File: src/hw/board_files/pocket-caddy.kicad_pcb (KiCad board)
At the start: 4 copper layers, 89 parts, among them J1 Conn_01x03_Pin, J2 Conn_01x03_Pin, J3 MSD-1-A, J4 Test_Points, P1 USB_C_Plug_USB2.0, Q1 PMOS, SW1 SW_PWR, SW2 RESET, SW3 BTN_2, SW4 BTN_1_BOOT, SW5 BTN_3, U1 FT234XD-R, U2 MCP73871, U3 TPS63031DSKR, U4 ESP32-C3-WROOM-02, U5 NEO-M9N, U6 BQ27427, U7 SHT30-DIS, Y1 32.768kHz

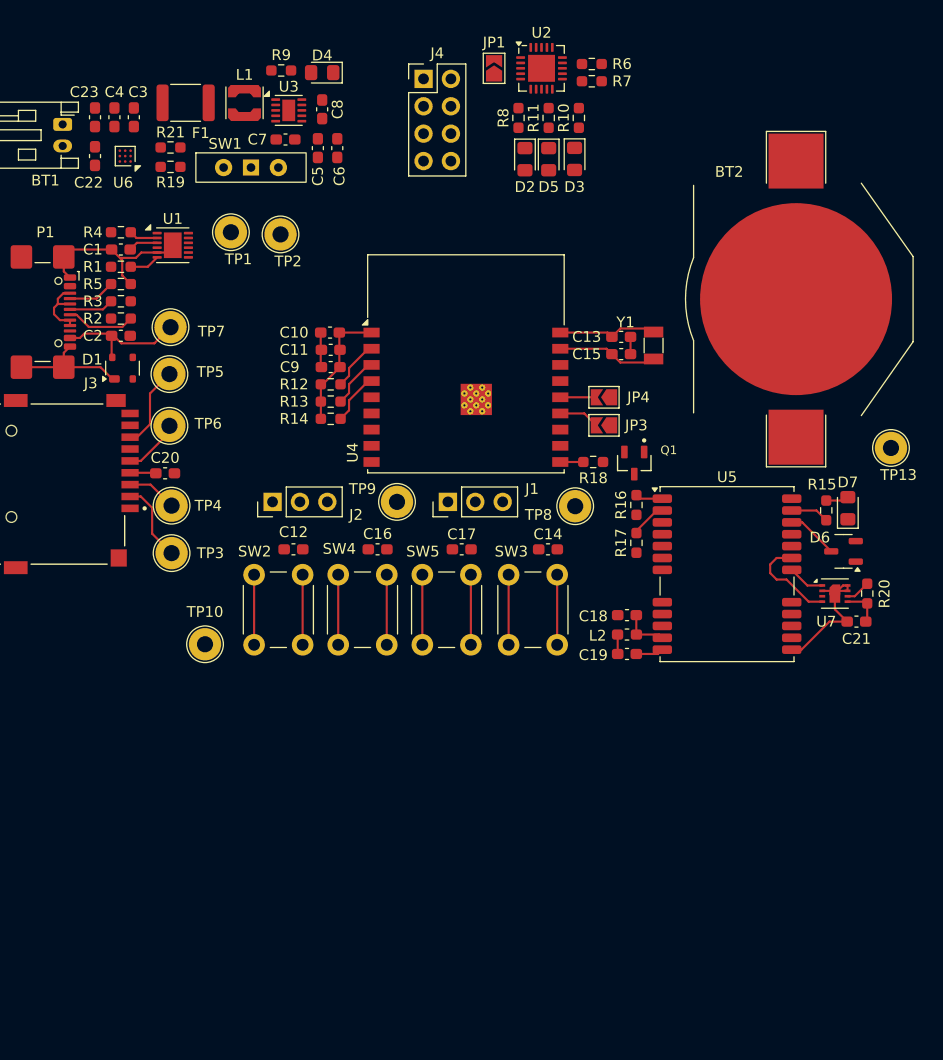
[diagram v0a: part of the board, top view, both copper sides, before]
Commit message: Added LCD to Schematic
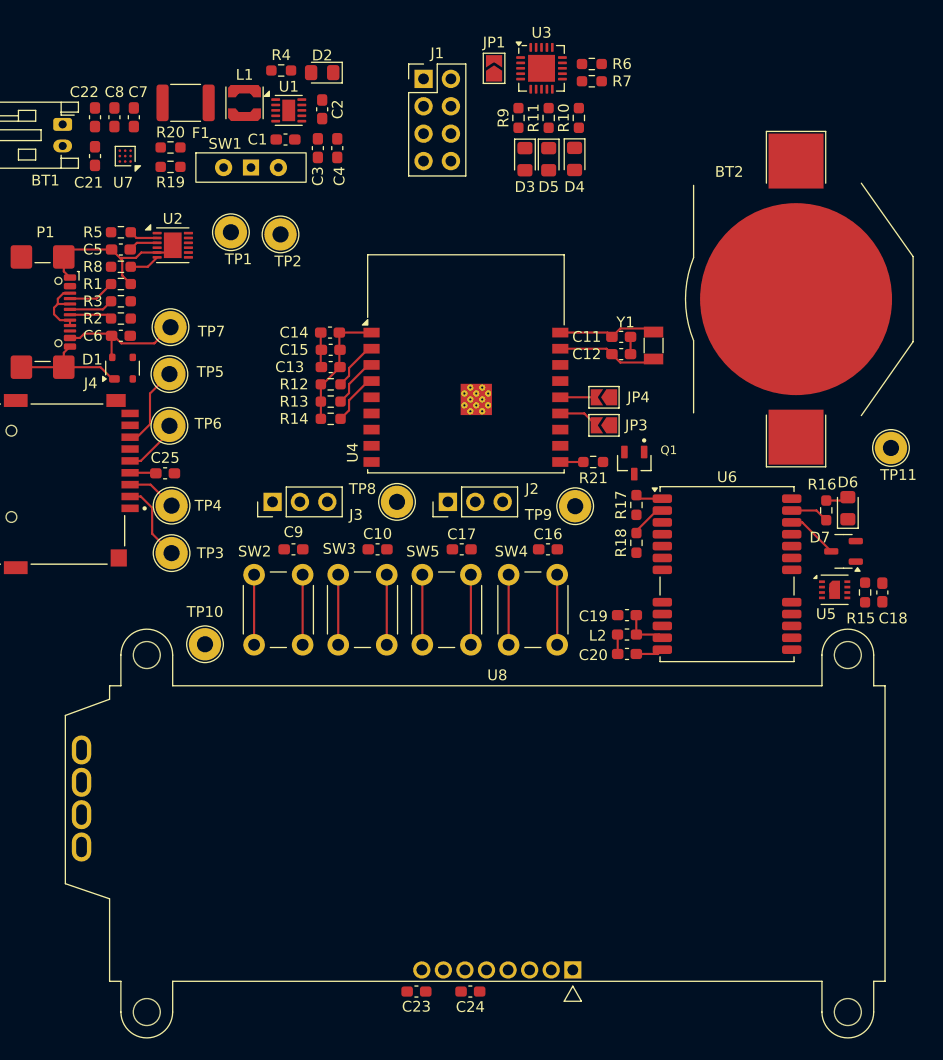
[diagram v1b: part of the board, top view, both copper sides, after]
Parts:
- added C23: 2u2, Capacitor_SMD:C_0603_1608Metric_Pad1.08x0.95mm_HandSolder, F.Cu at (71.2, 130.2)
- added C24: 1u, Capacitor_SMD:C_0603_1608Metric_Pad1.08x0.95mm_HandSolder, F.Cu at (76.2, 130.2)
- added U8: NHD-C0220BIZ-FSRGB, Display:NHD-C0220BiZ-FSRGB, F.Cu at (78.7, 112.3)
- moved C18 3.61 mm to (114.4, 93.2), turned to 90 degrees
- moved U5 0.35 mm to (110.0, 93.0)
- moved R15 0.22 mm to (112.8, 93.2), turned to -90 degrees
- turned R2 to 180 degrees
- renumbered C7 to C1, C16 to C10, C13 to C11, C15 to C12, C9 to C13, C10 to C14, C11 to C15, C14 to C16, C21 to C18, C18 to C19, C8 to C2, C19 to C20, C22 to C21, C23 to C22, C20 to C25, C5 to C3, C6 to C4, C1 to C5, C2 to C6, C3 to C7, C4 to C8, C12 to C9, D4 to D2, D2 to D3, D3 to D4, D7 to D6, D6 to D7, J4 to J1, J1 to J2, J2 to J3, J3 to J4, R5 to R1, R20 to R15, R15 to R16, R16 to R17, R17 to R18, R21 to R20, R18 to R21, R9 to R4, R4 to R5, R1 to R8, R8 to R9, SW4 to SW3, SW3 to SW4, TP13 to TP11, TP9 to TP8, TP8 to TP9, U3 to U1, U1 to U2, U2 to U3, U7 to U5, U5 to U6, U6 to U7
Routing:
- net GND: track 74.6 -> 61.5 mm
- net /SCL: track 13.8 -> 4.87 mm
- net +3V3: track 17.9 -> 14.3 mm
- net /SDA: track 8.19 -> 4.77 mm
- net Net-(D1-I/O2): track 6.42 -> 3.95 mm
- net Net-(U5-~{RESET}): track 2.31 -> 0.00 mm
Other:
- board text removed: "LCD SCREEN"

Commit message: Started working on layout traces
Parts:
- moved J1 6.78 mm to (73.8, 52.1), turned to 90 degrees
- moved R9 5.38 mm to (86.0, 48.5)
- moved D3 5.38 mm to (86.6, 52.3)
- moved D4 5.38 mm to (91.2, 52.3)
- moved D5 5.38 mm to (88.8, 52.3)
- moved JP1 5.38 mm to (83.7, 43.9)
- moved R10 5.38 mm to (91.6, 48.5)
- moved R11 5.38 mm to (88.8, 48.5)
- moved R6 5.38 mm to (92.8, 43.5)
- moved U3 5.38 mm to (88.1, 43.9)
- moved R7 5.38 mm to (92.8, 45.1)
- moved C3 3.70 mm to (65.7, 51.4)
- moved C4 3.70 mm to (67.5, 51.4)
- moved U1 3.70 mm to (63.0, 47.9)
- moved F1 3.70 mm to (53.5, 47.2)
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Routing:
- net GND: track 61.5 -> 86.4 mm, vias 0 -> 18
- net +3V3: track 14.3 -> 27.9 mm, vias 0 -> 10
- net /SD_CS: track 9.57 -> 2.14 mm
- net V_USB: track 12.7 -> 5.31 mm
- net /SPI_MISO: track 7.74 -> 0.65 mm
- net /SPI_SCK: track 5.35 -> 0.60 mm
- net /SPI_MOSI: track 4.66 -> 0.00 mm
- net Net-(U3-STAT1/~{LBO}): track 0.00 -> 4.44 mm
- net Net-(U4-EN): track 11.2 -> 14.9 mm
- net /Microcontroller/BTN_3: track 6.50 -> 10.3 mm
- net /Microcontroller/BTN_2: track 6.50 -> 10.3 mm
- net /Microcontroller/BTN_1_BOOT: track 6.50 -> 10.3 mm
- net Net-(U2-CBUS0): track 2.81 -> 0.00 mm
- net Net-(U2-3V3OUT): track 2.75 -> 0.00 mm
- net Net-(U2-~{RESET}): track 2.67 -> 0.00 mm
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- added copper zone on In1.Cu, net +3V3
- added copper zone on In2.Cu, net GND
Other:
- board outline added: 91.4 x 100 mm
- board text added: "+3V3"
- board text added: "Coin Cell Battery"
- board text added: "GND"
- board text added: "GPS Golf Caddy Rev. A B. Khun, B. York 10/6/25"
- board text added: "Li-Po Battery"
- board text added: "MISO"
- board text added: "MOSI"
- board text added: "Micro-SD Writter"
- board text added: "RX"
- board text added: "SCK"
- board text added: "SCL"
- board text added: "SDA"
- board text added: "SD_CS"
- board text added: "TX"
- board text added: "V-SYS"
- board text added: "VBAT"
- board text added: "V_BCKP"
- board text added: "V_USB"
- board text removed: "Antenna"
- board text removed: "LCD CONNECTOR"

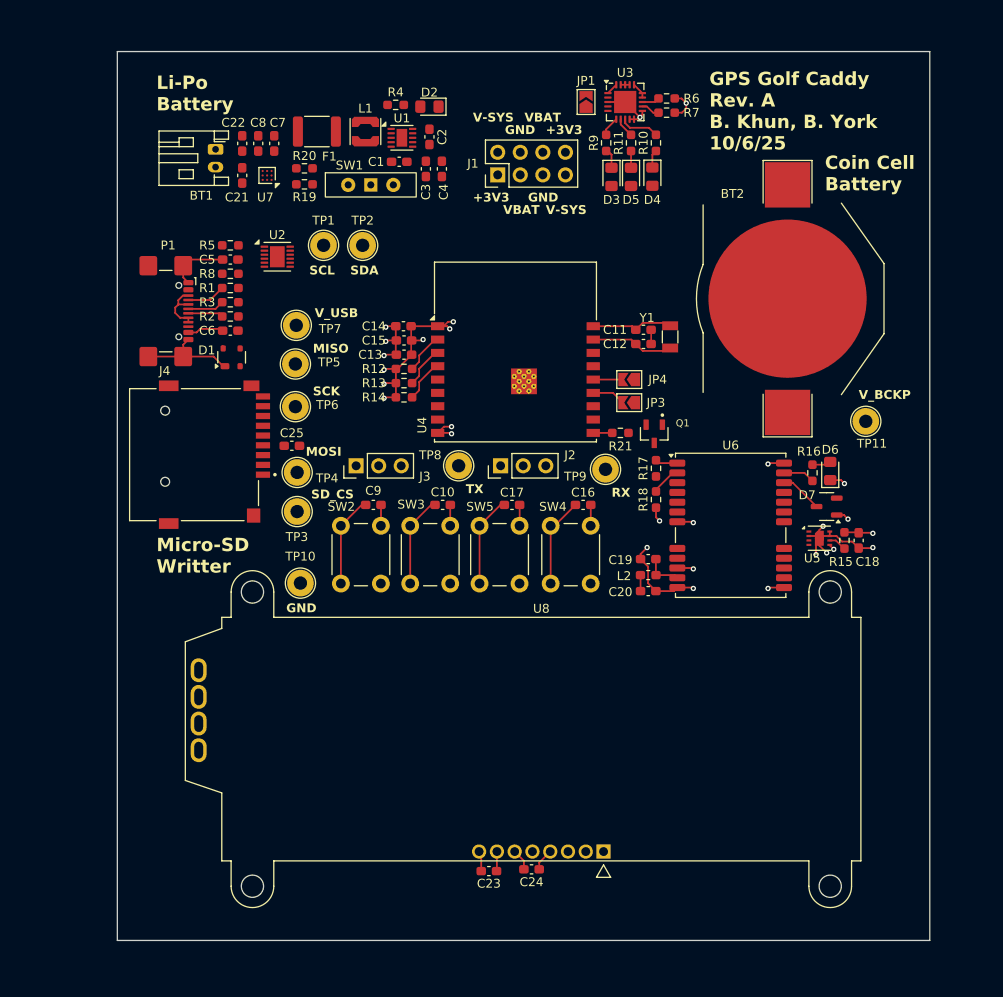
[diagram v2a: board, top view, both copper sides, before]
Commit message: Changed a footprint and made some minor changes.
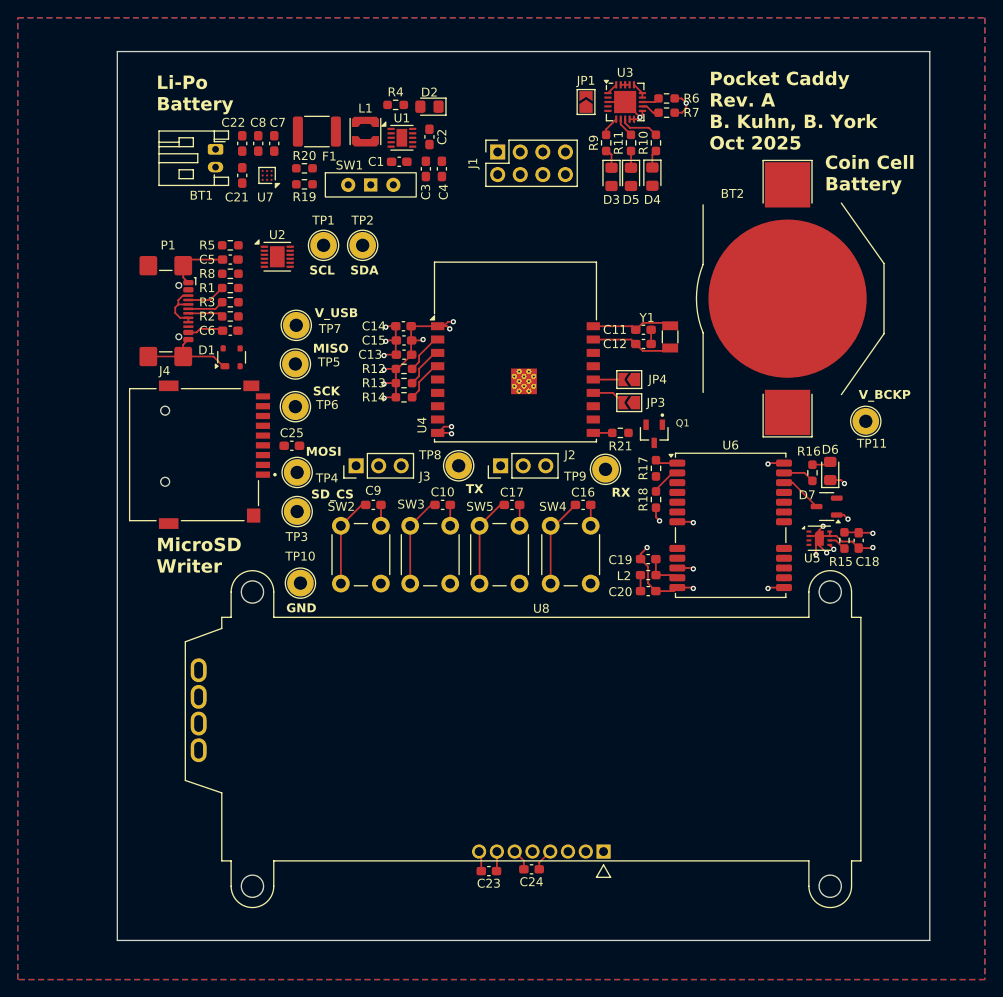
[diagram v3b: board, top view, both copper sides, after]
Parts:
- J1: footprint Connector_PinHeader_2.54mm:PinHeader_2x04_P2.54mm_Vertical -> Connector_PinSocket_2.54mm:PinSocket_2x04_P2.54mm_Vertical
- moved J1 2.58 mm to (73.8, 49.5)
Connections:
- J1 pad 2: V_SYS -> +3V3
- J1 pad 3: VBAT -> V_SYS
- J1 pad 4: GND -> V_SYS
- J1 pad 5: GND -> VBAT
- J1 pad 7: V_SYS -> GND
- J1 pad 8: +3V3 -> GND
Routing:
- added copper zone on B.Cu, net GND
- added copper zone on F.Cu, net GND
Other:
- board text added: "MicroSD Writer"
- board text added: "Pocket Caddy Rev. A B. Kuhn, B. York Oct 2025"
- board text removed: "+3V3"
- board text removed: "GPS Golf Caddy Rev. A B. Khun, B. York 10/6/25"
- board text removed: "Micro-SD Writter"
- board text removed: "V-SYS"
- board text removed: "VBAT"

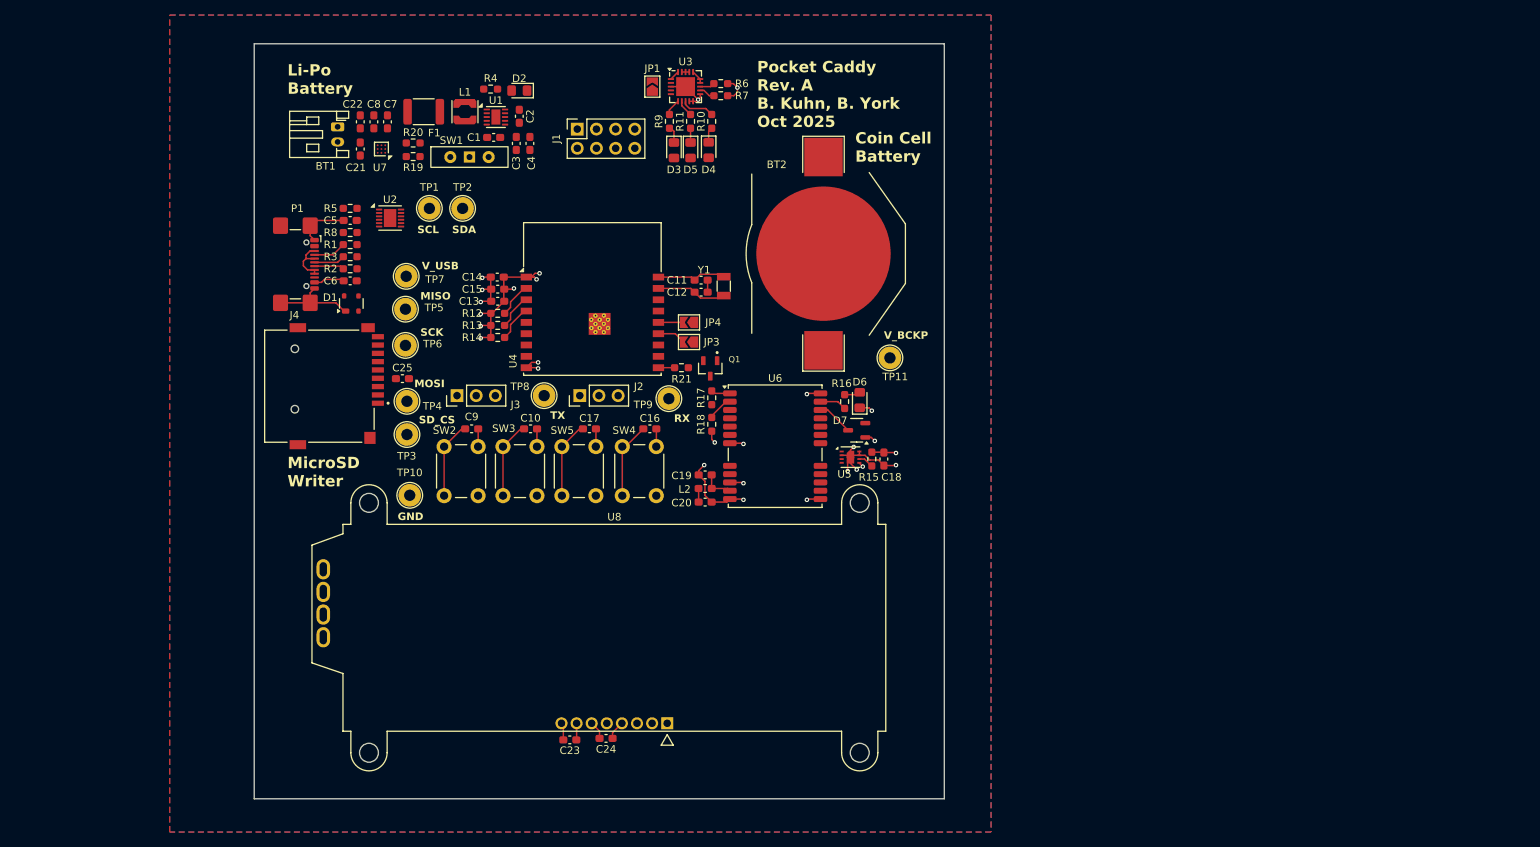
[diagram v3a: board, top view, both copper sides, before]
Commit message: Made antenna footprint. Making new branch to try new LCD and layout
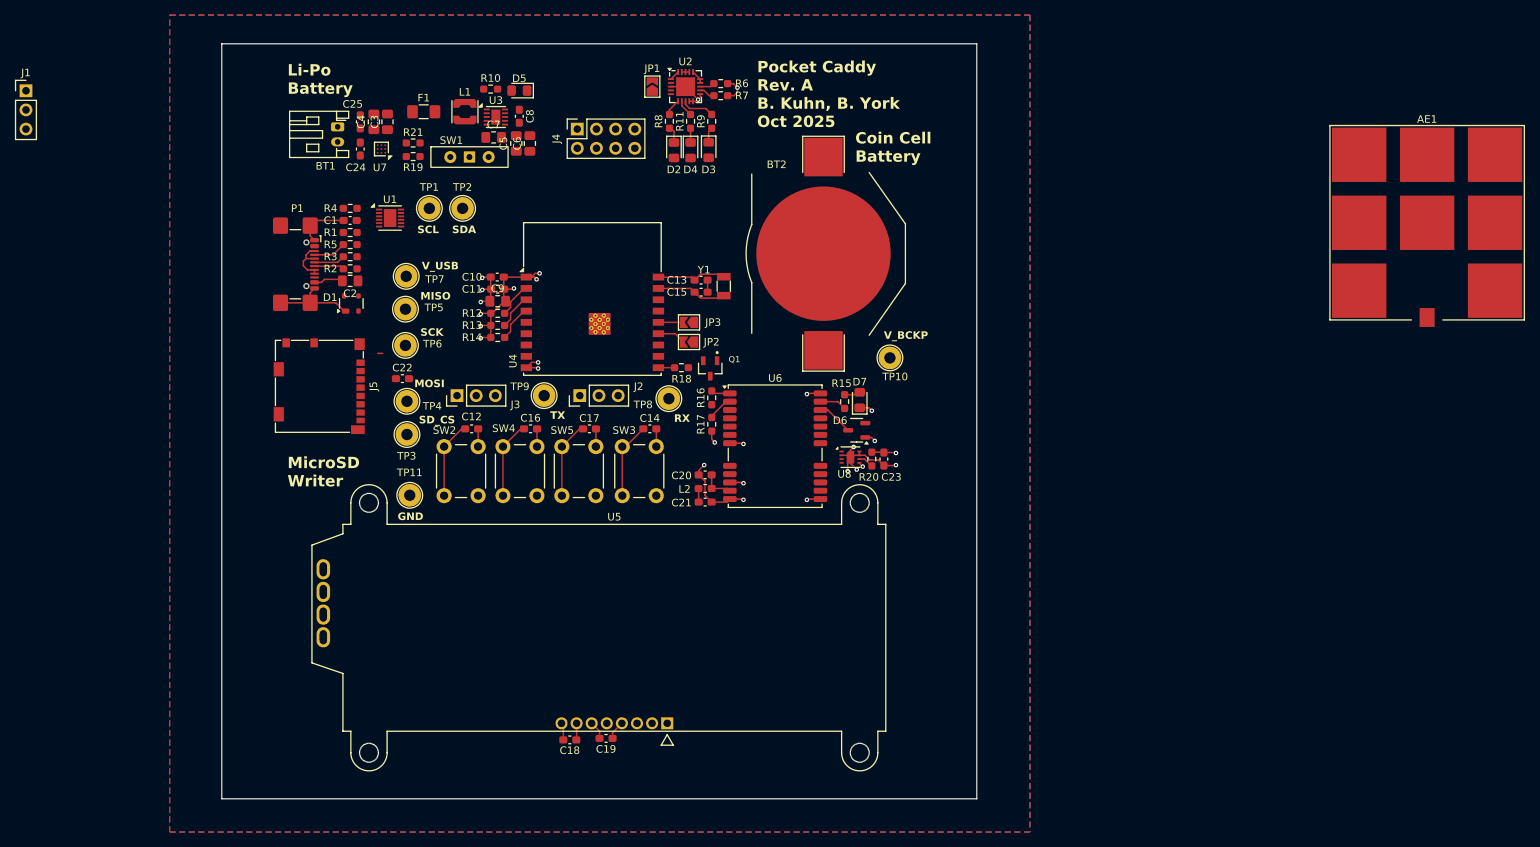
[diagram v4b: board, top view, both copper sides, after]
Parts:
- added AE1: SGGP.25.4.A.02, Project_Library:Antenna_Taoglas_SGGP.25.4.A.02_25x25mm, F.Cu at (186.3, 61.9)
- added J1: Conn_01x03_Pin, Connector_PinHeader_2.54mm:PinHeader_1x03_P2.54mm_Vertical, F.Cu at (0.77, 44.4)
- C2: renamed from C6; footprint Capacitor_SMD:C_0603_1608Metric_Pad1.08x0.95mm_HandSolder -> Capacitor_SMD:C_0805_2012Metric_Pad1.18x1.45mm_HandSolder
- C3: renamed from C7; footprint Capacitor_SMD:C_0603_1608Metric_Pad1.08x0.95mm_HandSolder -> Capacitor_SMD:C_0805_2012Metric_Pad1.18x1.45mm_HandSolder
- C4: renamed from C8; footprint Capacitor_SMD:C_0603_1608Metric_Pad1.08x0.95mm_HandSolder -> Capacitor_SMD:C_0805_2012Metric_Pad1.18x1.45mm_HandSolder
- C5: renamed from C3; footprint Capacitor_SMD:C_0603_1608Metric_Pad1.08x0.95mm_HandSolder -> Capacitor_SMD:C_0805_2012Metric_Pad1.18x1.45mm_HandSolder
- C6: renamed from C4; footprint Capacitor_SMD:C_0603_1608Metric_Pad1.08x0.95mm_HandSolder -> Capacitor_SMD:C_0805_2012Metric_Pad1.18x1.45mm_HandSolder
- C7: renamed from C1; footprint Capacitor_SMD:C_0603_1608Metric_Pad1.08x0.95mm_HandSolder -> Capacitor_SMD:C_0805_2012Metric_Pad1.18x1.45mm_HandSolder
- C9: renamed from C13; footprint Capacitor_SMD:C_0603_1608Metric_Pad1.08x0.95mm_HandSolder -> Capacitor_SMD:C_0805_2012Metric_Pad1.18x1.45mm_HandSolder
- F1: value 500mA -> 1A; footprint Fuse:Fuse_1812_4532Metric -> Fuse:Fuse_1206_3216Metric_Pad1.42x1.75mm_HandSolder
- J5: renamed from J4; value MSD-1-A -> Molex 104031-0811; footprint Library:CUI_MSD-1-A -> Connector_Card:microSD_HC_Molex_104031-0811
- L2: value 0 Ohm -> TBD
- renumbered C5 to C1, C14 to C10, C15 to C11, C9 to C12, C11 to C13, C16 to C14, C12 to C15, C10 to C16, C23 to C18, C24 to C19, C19 to C20, C20 to C21, C25 to C22, C18 to C23, C21 to C24, C22 to C25, C2 to C8, D3 to D2, D4 to D3, D5 to D4, D2 to D5, D7 to D6, D6 to D7, J1 to J4, JP3 to JP2, JP4 to JP3, R8 to R1, R4 to R10, R16 to R15, R17 to R16, R18 to R17, R21 to R18, R15 to R20, R20 to R21, R5 to R4, R1 to R5, R9 to R8, R10 to R9, SW4 to SW3, SW3 to SW4, TP11 to TP10, TP10 to TP11, TP9 to TP8, TP8 to TP9, U2 to U1, U3 to U2, U1 to U3, U8 to U5, U5 to U8
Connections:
- F1 pad 1: V_SYS -> Net-(J1-Pin_2)
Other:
- board size 91.4 x 100 mm -> 100 x 100 mm

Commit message: Moved some things around, revised regulator layout
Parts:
- removed BT1: LiPo, Connector_JST:JST_PH_S2B-PH-K_1x02_P2.00mm_Horizontal
- added H1: MountingHole_Pad, MountingHole:MountingHole_3.2mm_M3_Pad, F.Cu at (275.8, 28.9)
- added H2: MountingHole_Pad, MountingHole:MountingHole_3.2mm_M3_Pad, F.Cu at (275.8, 36.9)
- added H3: MountingHole_Pad, MountingHole:MountingHole_3.2mm_M3_Pad, F.Cu at (275.8, 44.8)
- added H4: MountingHole_Pad, MountingHole:MountingHole_3.2mm_M3_Pad, F.Cu at (275.8, 52.8)
- added H5: MountingHole_Pad, MountingHole:MountingHole_3.2mm_M3_Pad, F.Cu at (275.8, 60.7)
- added J6: Screw_Terminal_01x03, TerminalBlock_Phoenix:TerminalBlock_Phoenix_MPT-0,5-3-2.54_1x03_P2.54mm_Horizontal, F.Cu at (71.8, 25.6)
- added NT1: NetTie_2, NetTie:NetTie-2_SMD_Pad0.5mm, F.Cu at (-13.3, 46.5)
- moved Q1 111.6 mm to (202.0, 96.4), turned to 0 degrees
- moved R17 107.6 mm to (198.9, 80.9), turned to 180 degrees
- moved R16 107.3 mm to (198.9, 82.6), turned to 180 degrees
- moved C21 98.5 mm to (187.6, 80.9)
- moved C20 97.7 mm to (187.6, 82.7), turned to 0 degrees
- moved J4 97.3 mm to (-22.3, 34.4)
- moved L2 95.5 mm to (185.0, 81.8), turned to 90 degrees
- moved U6 90.9 mm to (190.9, 91.2), turned to -90 degrees
- moved TP1 84.0 mm to (-29.0, 48.9)
- moved TP11 84.0 mm to (-31.6, 86.8)
- moved TP2 84.0 mm to (-24.6, 48.9)
- moved TP3 84.0 mm to (-32.0, 78.8)
- moved TP4 84.0 mm to (-32.0, 74.4)
- moved TP5 84.0 mm to (-32.2, 62.2)
- moved TP6 84.0 mm to (-32.2, 67.0)
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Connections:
- AE1 pad 1: GND -> Net-(AE1-FEED)
- AE1 pad MP: (no net) -> GND
- C21 pad 1: Net-(AE1-PCB_Trace) -> Net-(AE1-FEED)
- L2 pad 2: Net-(AE1-PCB_Trace) -> Net-(AE1-FEED)
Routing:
- net /USB-C and Power/NTC_THERM: track 0.00 -> 18.3 mm, vias 0 -> 1
- net Net-(AE1-FEED): track 0.00 -> 15.1 mm
- net GND: track 86.4 -> 72.2 mm, vias 18 -> 23
- net +3V3: track 27.9 -> 34.4 mm, vias 10 -> 12
- net PGND: track 0.00 -> 4.49 mm, vias 0 -> 3
- net Net-(U3-EN): track 0.00 -> 4.13 mm
- net Net-(SW1-B): track 0.00 -> 3.52 mm
- net Net-(U2-~{PG}): track 2.22 -> 4.59 mm
- net Net-(D5-A): track 0.00 -> 2.17 mm
- net VBAT: track 1.83 -> 0.00 mm
- net Net-(AE1-PCB_Trace): track 1.81 -> 0.00 mm
- net Net-(U2-PROG3): track 2.10 -> 3.72 mm
- net V_SYS: track 1.33 -> 0.00 mm
- net Net-(U2-STAT1/~{LBO}): track 4.44 -> 5.72 mm
- net Net-(U3-L2): track 0.00 -> 1.02 mm
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- added copper zone on F.Cu, net +3V3
- added copper zone on In2.Cu, net +3V3
- added copper zone on In1.Cu, net GND
- added copper zone on F.Cu, net Net-(SW1-A)
- added copper zone on F.Cu, net Net-(U3-EN)
- added copper zone on F.Cu, net Net-(U3-L1)
- added copper zone on F.Cu, net Net-(U3-L2)
- added copper zone on F.Cu, net PGND
- removed copper zone on In1.Cu, net +3V3
- removed copper zone on In2.Cu, net GND
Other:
- outline, holes or cut-outs redrawn
- board text removed: "MISO"
- board text removed: "MOSI"
- board text removed: "MicroSD Writer"
- board text removed: "RX"
- board text removed: "SCK"
- board text removed: "SCL"
- board text removed: "SDA"
- board text removed: "SD_CS"
- board text removed: "TX"
- board text removed: "V_USB"
